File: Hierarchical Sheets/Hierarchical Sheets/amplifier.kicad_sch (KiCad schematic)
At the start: 3 parts, among them U2 ${SIM.PARAMS}

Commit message: Update .gitignore update PCB footprints
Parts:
- R10, R2: footprint (none) -> Resistor_SMD:R_0201_0603Metric_Pad0.64x0.40mm_HandSolder
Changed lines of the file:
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@@
 			)
 		)
-		(property "Footprint" ""
+		(property "Footprint" "Resistor_SMD:R_0201_0603Metric_Pad0.64x0.40mm_HandSolder"
 			(at 120.65 69.088 90)
 			(effects
@@
 			)
 		)
-		(property "Footprint" ""
+		(property "Footprint" "Resistor_SMD:R_0201_0603Metric_Pad0.64x0.40mm_HandSolder"
 			(at 133.35 49.022 90)
 			(effects

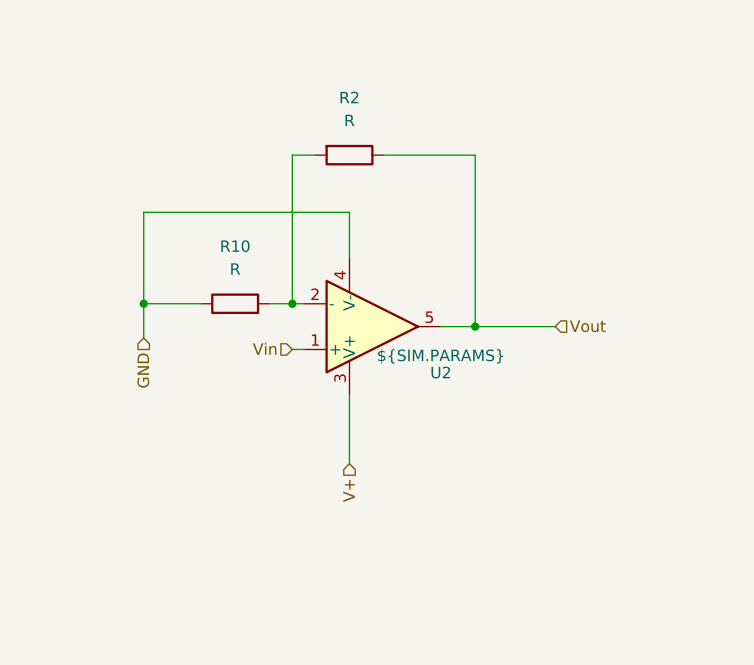
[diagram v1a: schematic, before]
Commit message: layout of amplifier 1 - begin
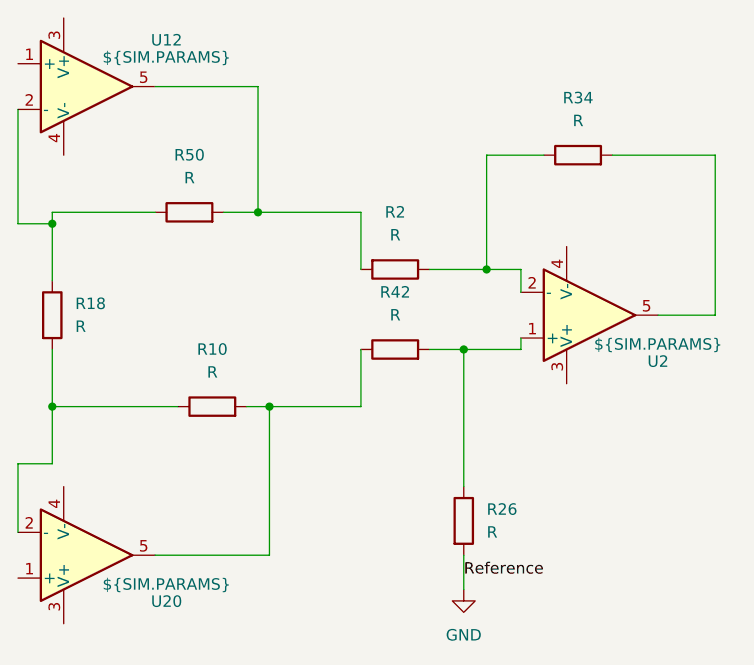
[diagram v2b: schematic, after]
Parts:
- added R18, R26, R34, R42, R50: R, symbol Device:R
- added U12, U20: ${SIM.PARAMS}, symbol Simulation_SPICE:OPAMP
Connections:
- net GND: now also R26.2; no longer R10.1, U2.4 (V-)
- net V+: no longer names the net of U2.3 (V+)
- net Vin: no longer names the net of U2.1 (+)
- net Vin: now also R26.1, R42.2
- net Vout: no longer names the net of R2.1
- net Vout: now also U2.2 (-), R34.1; no longer U2.5
- new net: R10.1, R18.2, U20.2 (-)
- new net: R10.2, R42.1, U20.5
- new net: R34.2, U2.5
- new net: R18.1, R50.1, U12.2 (-)
- new net: R2.2, R50.2, U12.5
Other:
- moved on the sheet: R10, R2, U2

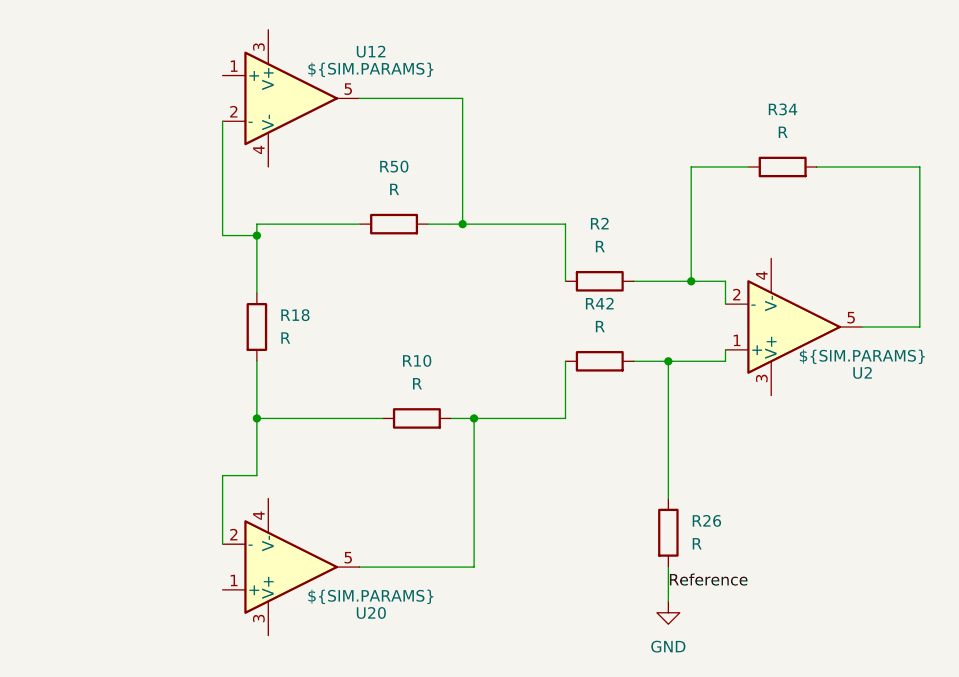
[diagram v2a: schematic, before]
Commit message: Continued researching IA topologies and design strategies -- updated amplifier schematics with 2 Op Amp topology
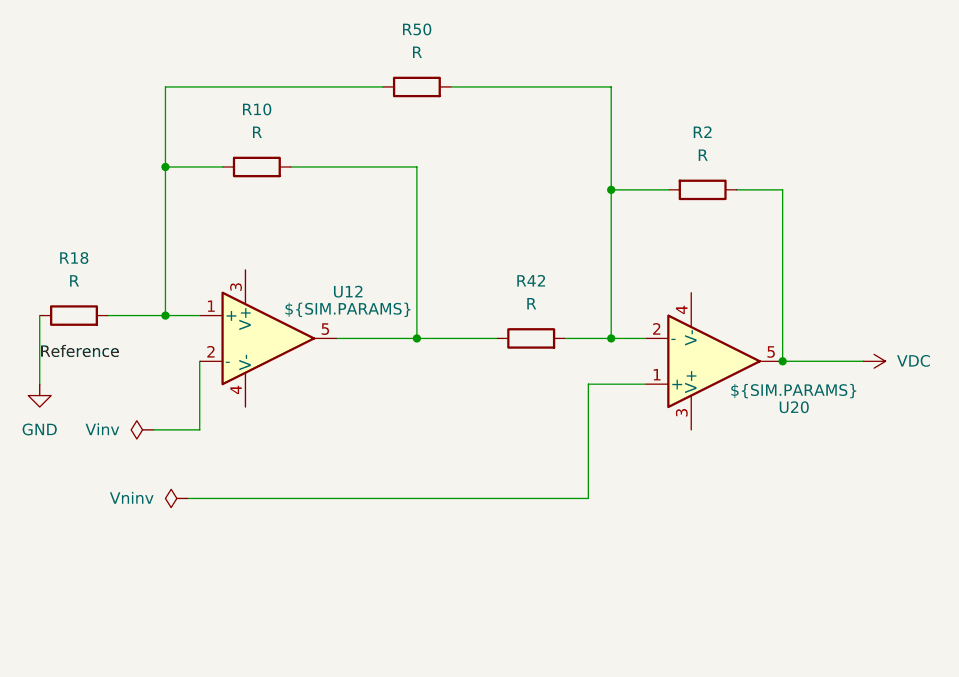
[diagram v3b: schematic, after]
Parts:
- removed R26, R34: R, symbol Device:R
- removed U2: ${SIM.PARAMS}, symbol Simulation_SPICE:OPAMP
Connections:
- net GND: now also R18.1
- net at R10.1, R18.2: now also R50.1, U12.1 (+); no longer U20.2 (-)
- net at R10.2, R42.1: now also U12.5; no longer U20.5
- net at R42.2: now also R2.2, R50.2, U20.2 (-)
- net VDC: now reaches R2.1
- net VDC: now also U20.5
- now unconnected: U12.2 (-)
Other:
- moved on the sheet: R10, R18, R2, R42, R50, U12, U20

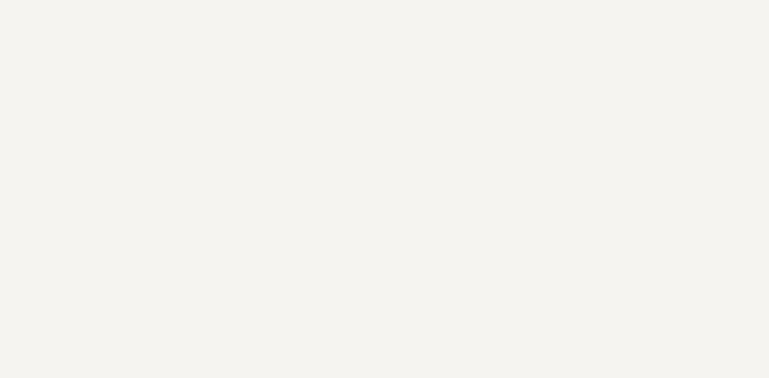
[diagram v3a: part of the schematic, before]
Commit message: Cited a source for the instr amp topology
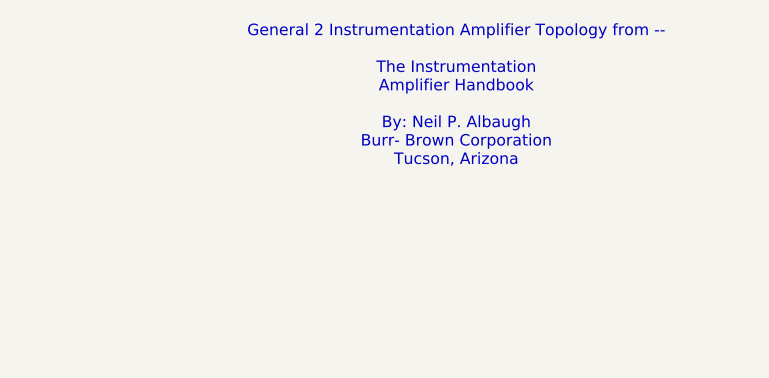
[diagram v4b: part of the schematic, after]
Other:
- note added: "General 2 Instrumentation Amplifier Topology from -- The Instrumentation Amplifier Handbook By: Neil P. Albaugh Burr- Brown Corporation Tucson, Arizona"
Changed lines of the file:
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@@
 	(generator_version "9.0")
 	(paper "A4")
+	(text "General 2 Instrumentation Amplifier Topology from --\n\nThe Instrumentation\nAmplifier Handbook\n\nBy: Neil P. Albaugh\nBurr- Brown Corporation\nTucson, Arizona"
+		(exclude_from_sim no)
+		(at 250.952 30.48 0)
+		(effects
+			(font
+				(size 1.27 1.27)
+			)
+		)
+	)
 	(junction
 		(at 158.75 72.39)

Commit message: Contined looking into topologies and general op amp information - added notes to amplifier schematics.
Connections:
- net at R10.1, R18.2, R50.1: now also U12.2 (-); no longer U12.1 (+)
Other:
- note added: "Need Transducer Specs: voltage swing, output impedance, etc."
- note added: "Used 2 op amp topology to minimize cost compared to the 3 op amp topology while maintaining the high input impedance to prevent current draw from the battery supply."
